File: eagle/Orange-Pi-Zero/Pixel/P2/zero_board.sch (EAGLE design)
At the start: 13 parts, among them CN1 1X4-3.5MM, IC1 74HCT125N, J1 1X2-3.5MM

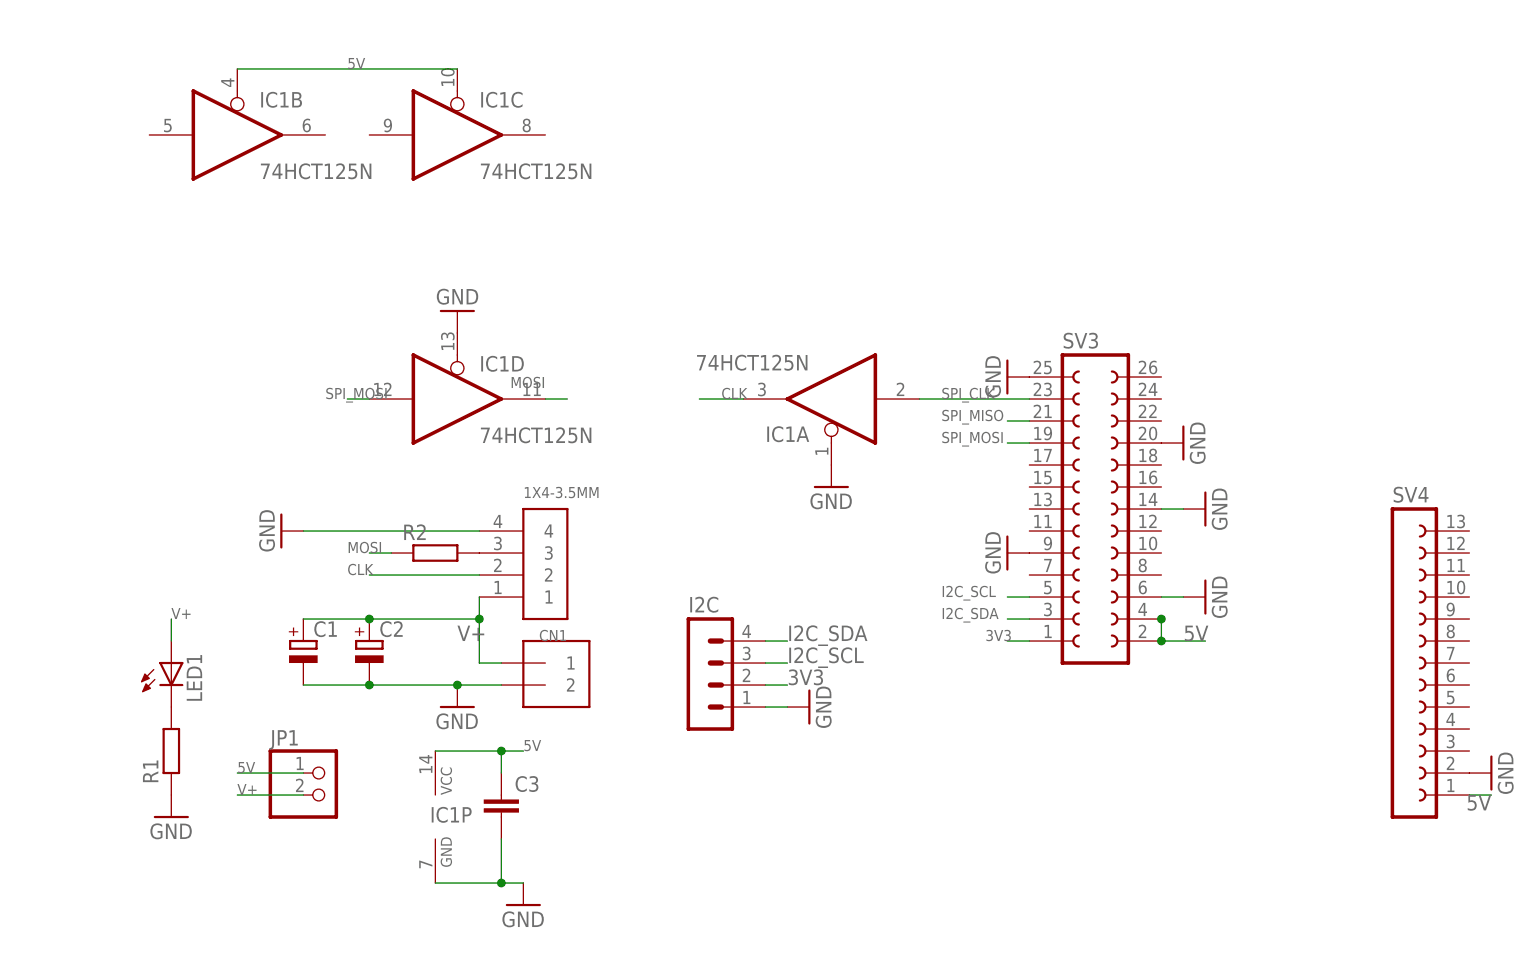
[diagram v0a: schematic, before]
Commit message: Removed pixel driver prototype V1
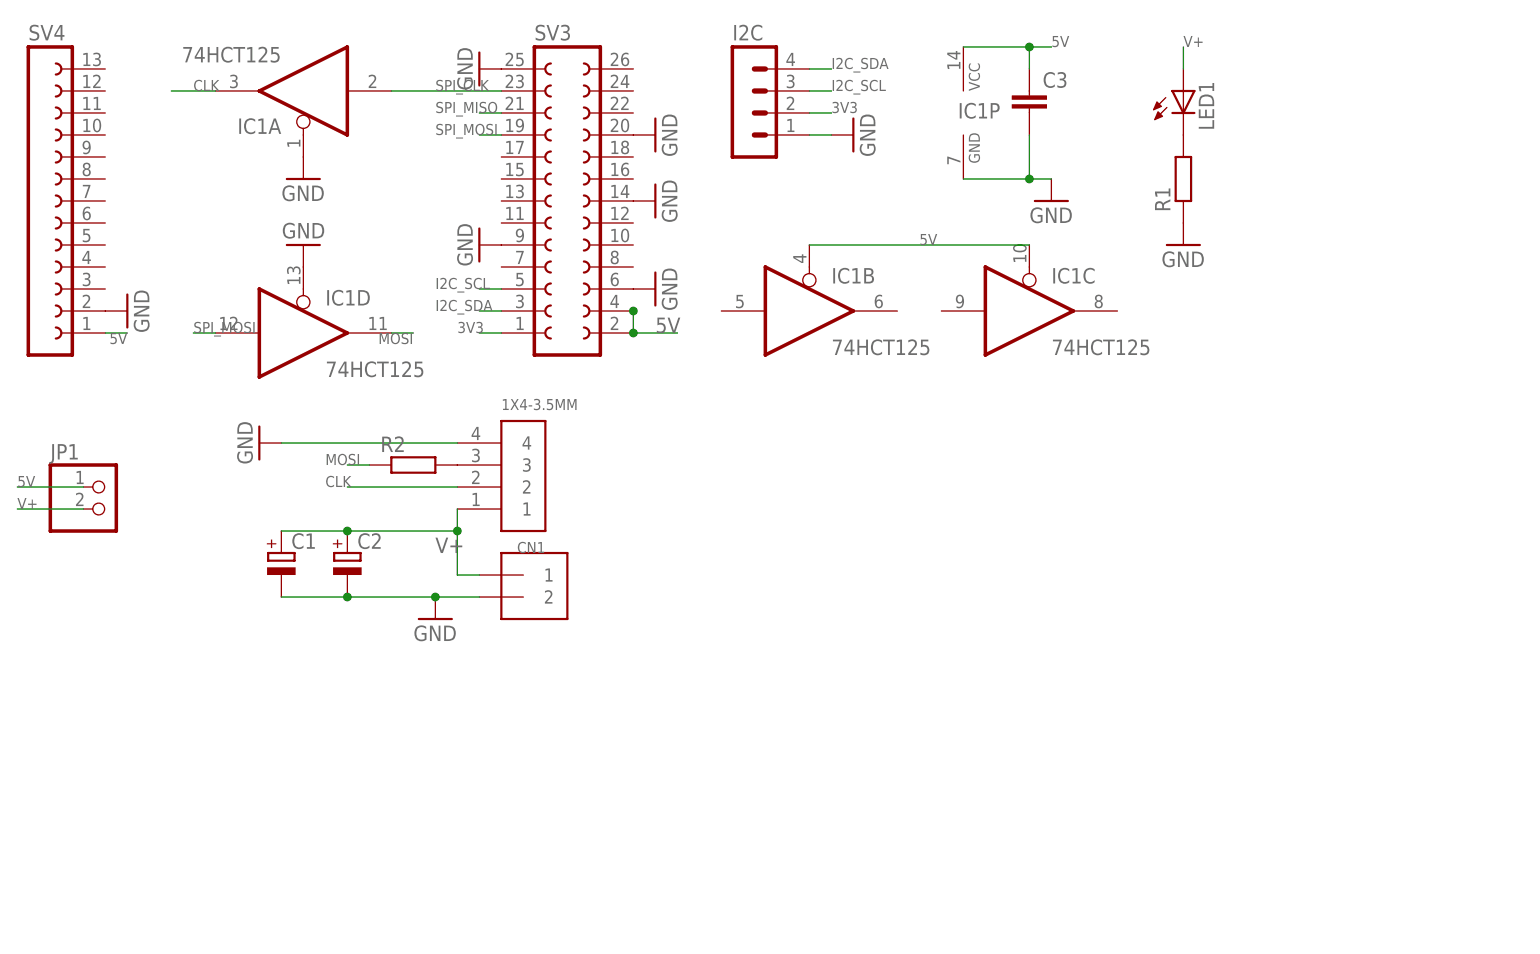
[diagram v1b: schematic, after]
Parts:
- IC1: value 74HCT125N -> 74HCT125
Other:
- moved on the sheet: C1, C2, C3, CN1, I2C, IC1A, IC1B, IC1C, IC1D, IC1P, JP1, LED1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

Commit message: Updates
Work in progress -> http://www.orangepi-dmx.org/pixel-boards
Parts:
- removed I2C: (no value), con-lstb:MA04-1
- added SV2: OPi Zero 2x13, con-lsta:FE13-2
- C1, C2: value (none) -> 1000u
- C3: value (none) -> 100n
- JP1: value (none) -> jumper
- LED1: value (none) -> 3mm
- R1, R2: value (none) -> 330
- SV1: value (none) -> OPi Zero 1x13
- SV3: value (none) -> I2C-OLED; device con-lsta:FE13-2 -> con-lstb:MA04-1
- renumbered SV4 to SV1
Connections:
- removed net SPI_MISO: SV3.21
- net 3V3: now also SV2.1, SV3.2; no longer I2C.2, SV3.1
- net 5V: now also SV2.2, SV2.4; no longer SV3.2, SV3.4
- net GND: now also R2.1, SV2.14, SV2.20, SV2.25, SV2.6, SV2.9, SV3.1; no longer I2C.1, R1.1, SV3.14, SV3.20, SV3.25, SV3.6, SV3.9
- net I2C_SCL: now also SV2.5, SV3.3; no longer I2C.3, SV3.5
- net I2C_SDA: now also SV2.3, SV3.4; no longer I2C.4, SV3.3
- net MOSI: now also R1.1; no longer R2.1
- net N$1: now also R2.2; no longer R1.2
- net N$2: now also R1.2; no longer R2.2
- net SPI_CLK: now also SV2.23; no longer SV3.23
- net SPI_MOSI: now also SV2.19; no longer SV3.19
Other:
- moved on the sheet: R1, R2
